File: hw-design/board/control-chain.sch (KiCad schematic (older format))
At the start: 17 parts, among them J1 CC_INPUT, J2 CC_OUTPUT, Q4 2N7002, Q5 2N7002, Q6 RFML8244TRPBF, U3 ISL83491

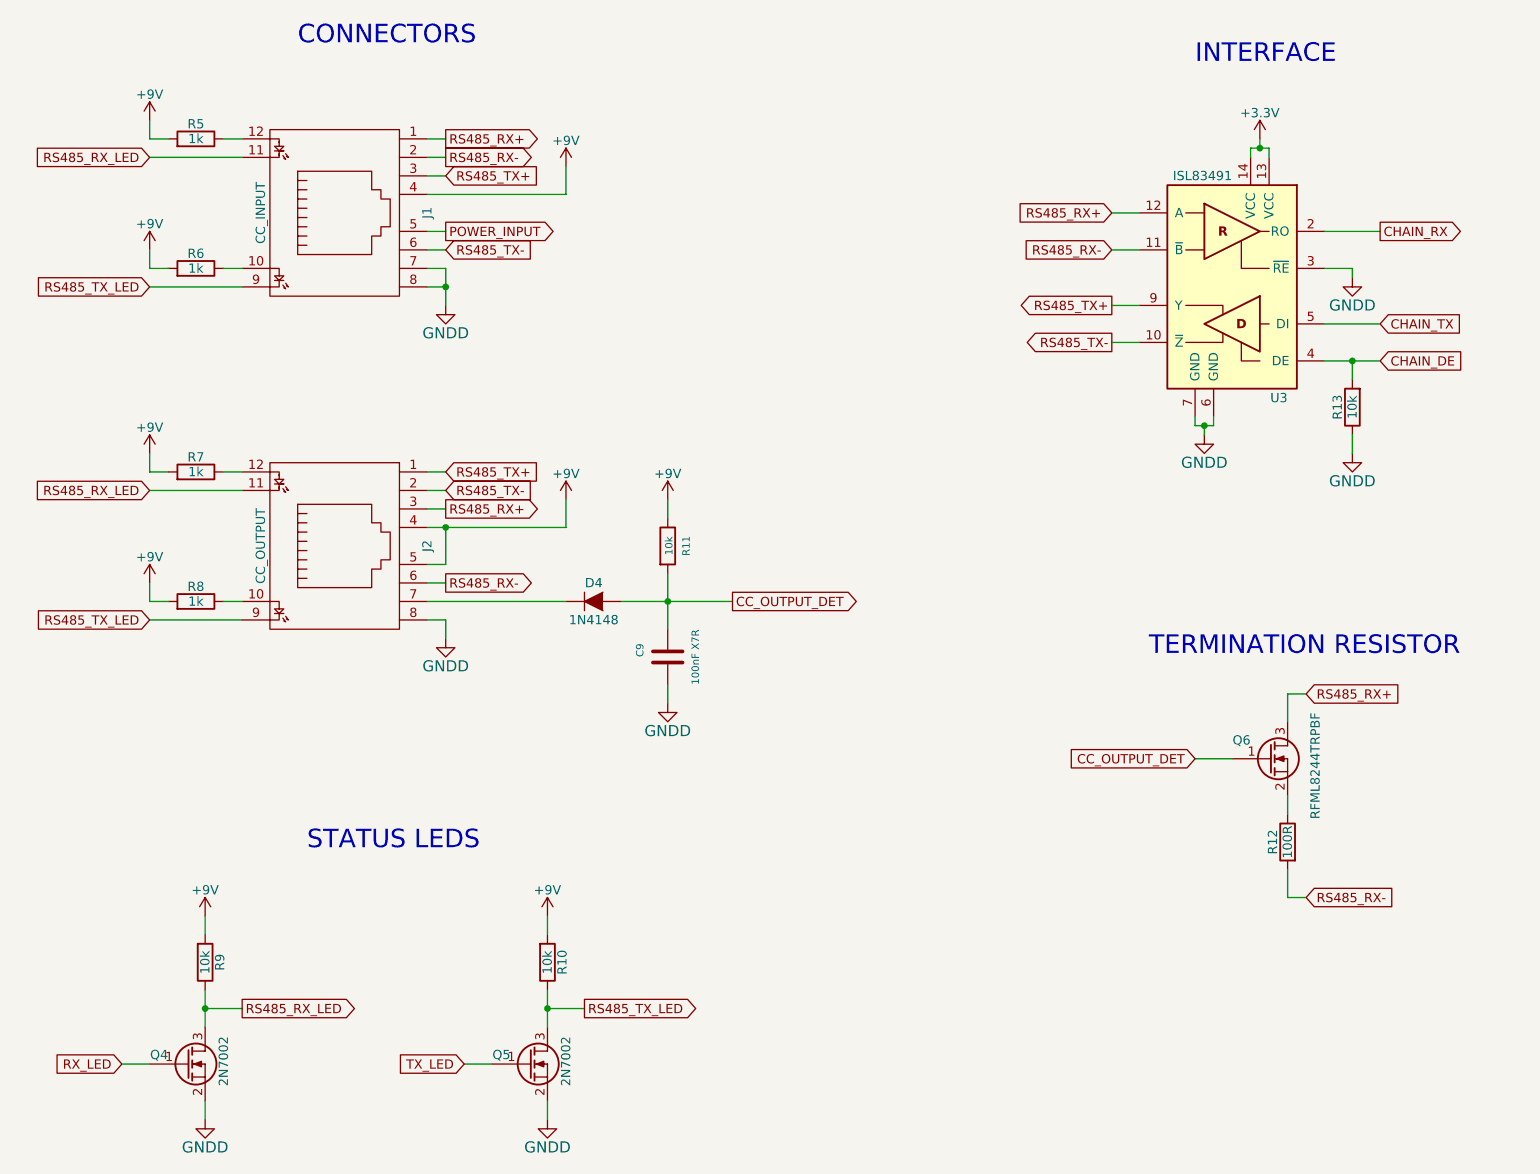
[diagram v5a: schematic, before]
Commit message: sch: adding values and MPN to components
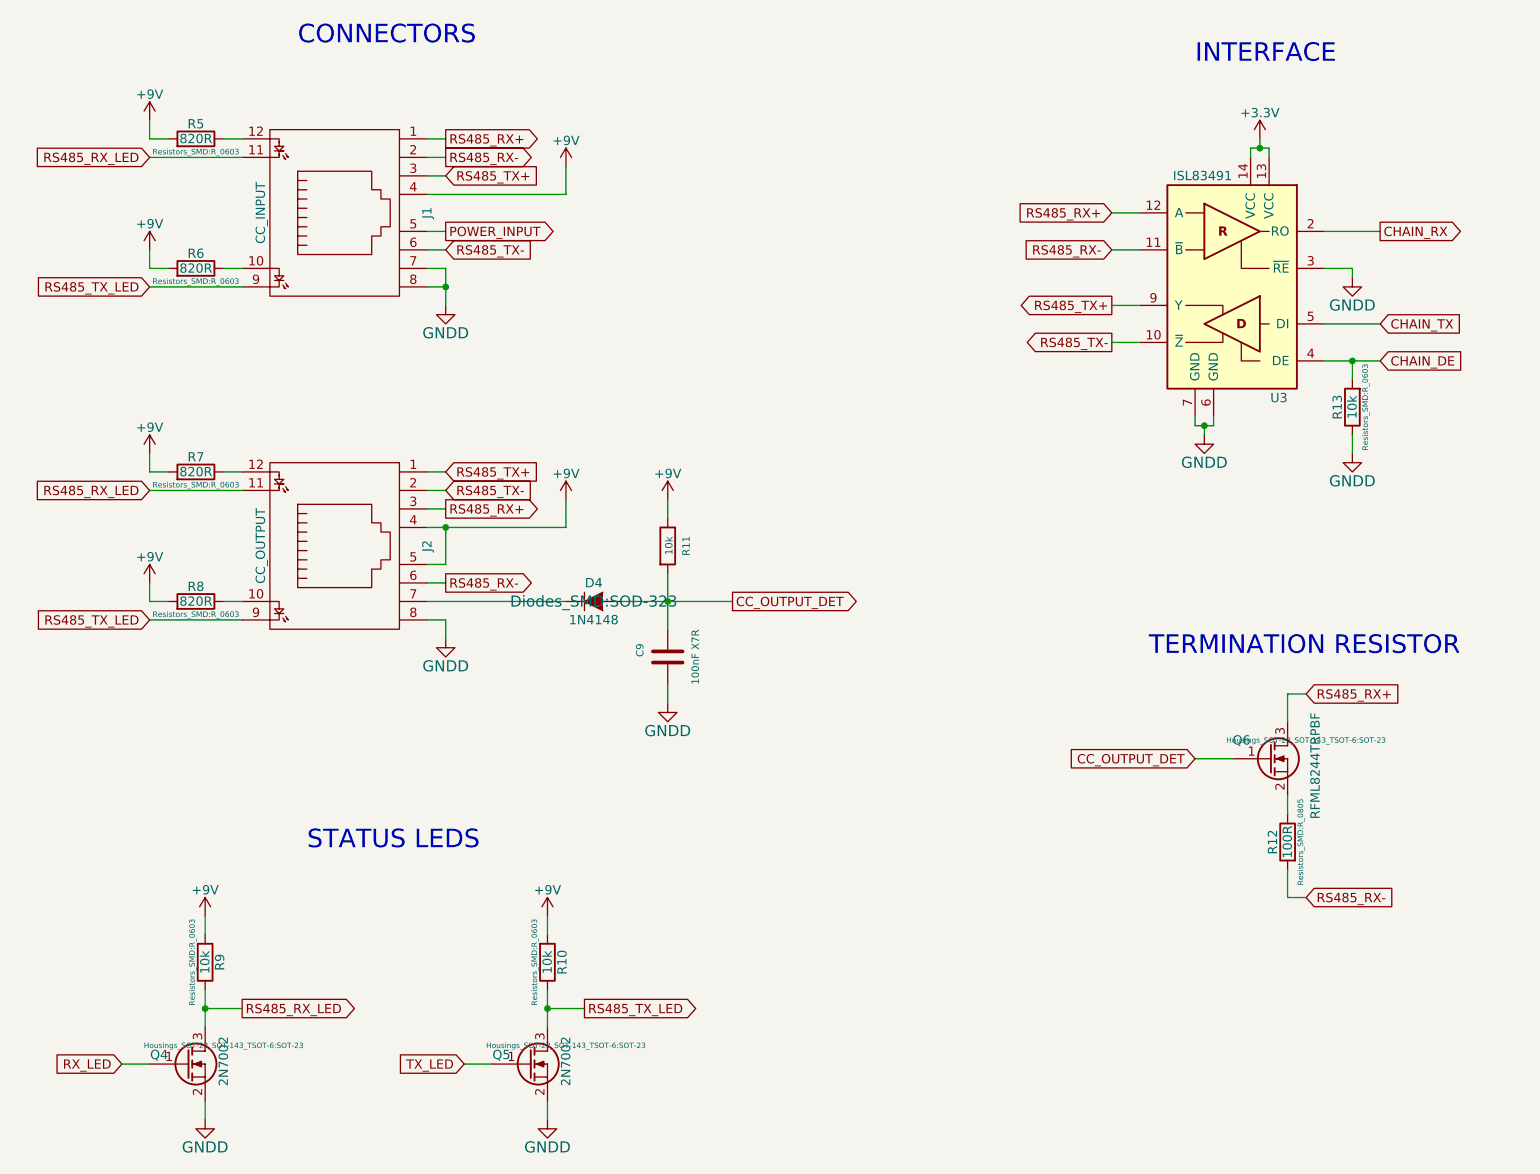
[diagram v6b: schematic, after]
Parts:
- C9: MPN (none) -> C1608X7R1E104K080AA
- D4: footprint (none) -> Diodes_SMD:SOD-323; MPN (none) -> 1N4148WX-TP
- J1, J2: MPN (none) -> RJHSE-5381
- Q4, Q5: footprint (none) -> Housings_SOT-23_SOT-143_TSOT-6:SOT-23; MPN (none) -> 2N7002P,215
- Q6: footprint (none) -> Housings_SOT-23_SOT-143_TSOT-6:SOT-23; MPN (none) -> RFML8244TRPBF
- R10, R13, R9: footprint (none) -> Resistors_SMD:R_0603; MPN (none) -> RMCF0603JT10K0
- R11: MPN (none) -> RMCF0603JT10K0
- R12: footprint (none) -> Resistors_SMD:R_0805; MPN (none) -> ERJ-P06F1000V
- R5, R6, R7, R8: value 1k -> 820R; footprint (none) -> Resistors_SMD:R_0603; MPN (none) -> ESR03EZPJ821
- U3: footprint (none) -> Housings_SOIC:SOIC-14_3.9x8.7mm_Pitch1.27mm; MPN (none) -> ISL83491IBZ

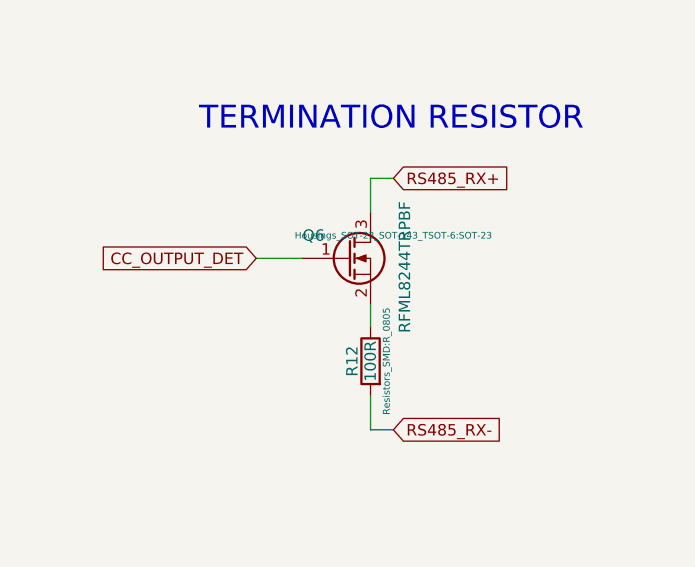
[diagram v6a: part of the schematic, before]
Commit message: sch: MOSFET MPN fixed
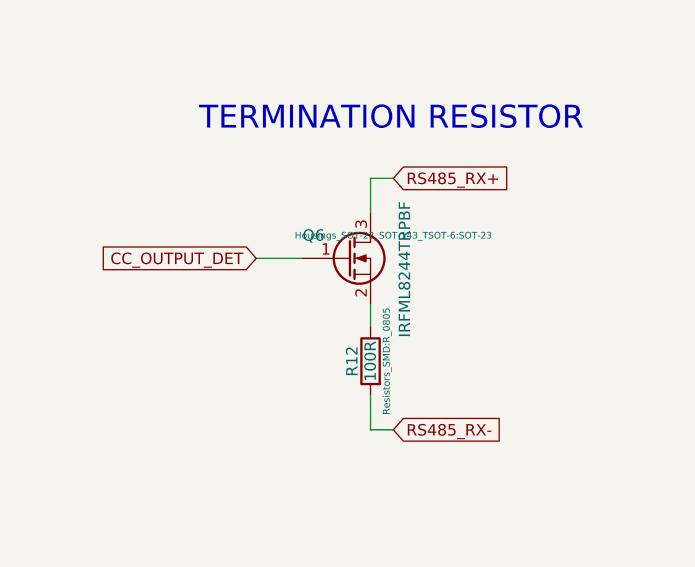
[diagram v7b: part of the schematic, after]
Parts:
- Q6: value RFML8244TRPBF -> IRFML8244TRPBF; MPN RFML8244TRPBF -> IRFML8244TRPBF
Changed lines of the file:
@@
 P 8200 4950
 F 0 "Q6" H 8100 5050 50  0000 R CNN
-F 1 "RFML8244TRPBF" V 8450 5200 50  0000 R CNN
+F 1 "IRFML8244TRPBF" V 8450 5200 50  0000 R CNN
 F 2 "Housings_SOT-23_SOT-143_TSOT-6:SOT-23" H 8400 5050 29  0000 C CNN
 F 3 "" H 8200 4950 60  0000 C CNN
-F 4 "RFML8244TRPBF" H 0   0   50  0001 C CNN "MPN"
+F 4 "IRFML8244TRPBF" H 0   0   50  0001 C CNN "MPN"
 	1    8200 4950
 	1    0    0    -1

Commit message: sch: setting footprints and updating BOM
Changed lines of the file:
@@
 F 0 "U3" H 7700 1800 50  0000 L CNN
 F 1 "ISL83491" H 8000 3000 50  0000 L CNN
-F 2 "Housings_SOIC:SOIC-14_3.9x8.7mm_Pitch1.27mm" H 8000 2400 50  0001 C CIN
+F 2 "Housings_SOIC:SOIC-14_3.9x8.7mm_Pitch1.27mm" H 8000 2400 50  0000 C CIN
 F 3 "" H 8000 2400 60  0000 C CNN
 F 4 "ISL83491IBZ" H 0   0   50  0001 C CNN "MPN"
